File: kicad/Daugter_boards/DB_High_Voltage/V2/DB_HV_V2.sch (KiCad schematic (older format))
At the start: 5 parts, among them P1 CONN_01X19, P2 BNC, P3 CONN_01X19, U1 Recom

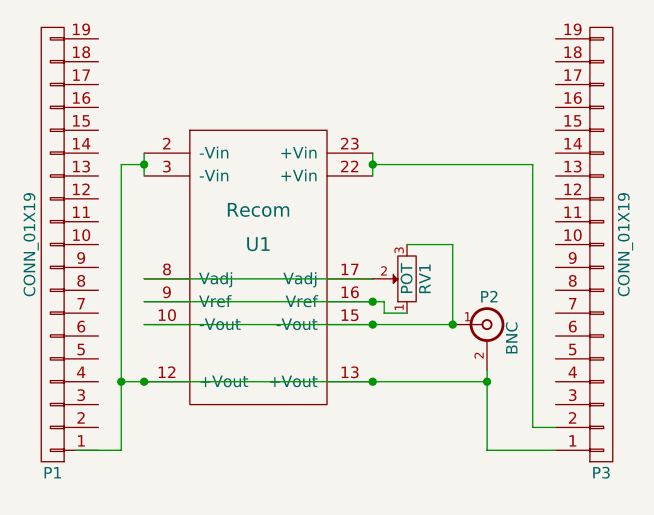
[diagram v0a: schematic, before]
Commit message: adding DB_Filter
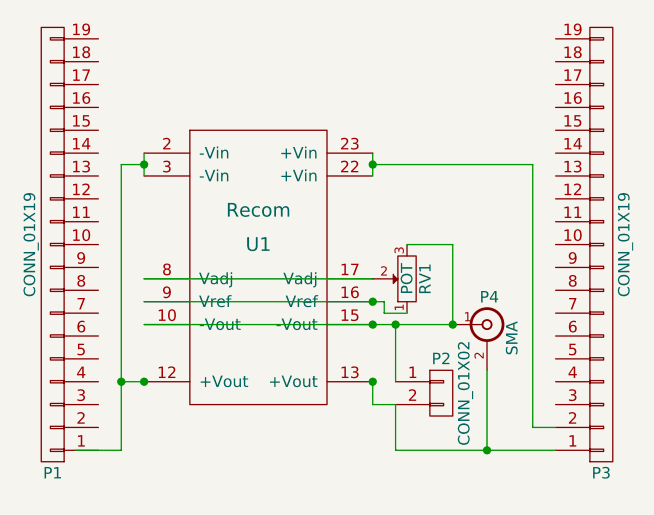
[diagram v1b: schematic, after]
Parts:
- removed P2: BNC, symbol BNC
- added P2: CONN_01X02, symbol CONN_01X02
- added P4: SMA, symbol SMA
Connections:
- wire segments 18 -> 22
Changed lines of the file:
@@
 LIBS:valves
 LIBS:echopen
+LIBS:DB_HV_V2-cache
 EELAYER 25 0
 EELAYER END
@@
 Wire Wire Line
 	4450 3350 5800 3350
-Wire Wire Line
-	4350 3600 5950 3600
 Wire Wire Line
 	4450 2650 4350 2650
@@
 	4350 3900 4150 3900
 Connection ~ 4350 3600
-$Comp
-L BNC P2
-U 1 1 57A84EE9
-P 5950 3350
-F 0 "P2" H 5960 3470 50  0000 C CNN
-F 1 "BNC" V 6060 3290 50  0000 C CNN
-F 2 "" H 5950 3350 50  0000 C CNN
-F 3 "" H 5950 3350 50  0000 C CNN
-	1    5950 3350
-	1    0    0    -1
-$EndComp
-Wire Wire Line
-	5950 3550 5950 3900
 Connection ~ 5450 3600
 $Comp
@@
 $EndComp
 Wire Wire Line
-	5950 3900 6250 3900
-Connection ~ 5950 3600
+	5550 3900 6250 3900
 Wire Wire Line
 	6150 2650 6150 3800
 Wire Wire Line
 	6150 3800 6250 3800
+$Comp
+L SMA P4
+U 1 1 57A87B90
+P 5950 3350
+F 0 "P4" H 5960 3470 50  0000 C CNN
+F 1 "SMA" V 6060 3290 50  0000 C CNN
+F 2 "" H 5950 3350 50  0000 C CNN
+F 3 "" H 5950 3350 50  0000 C CNN
+	1    5950 3350
+	1    0    0    -1
+$EndComp
+$Comp
+L CONN_01X02 P2
+U 1 1 57A87C25
+P 5750 3650
+F 0 "P2" H 5750 3800 50  0000 C CNN
+F 1 "CONN_01X02" V 5850 3650 50  0000 C CNN
+F 2 "" H 5750 3650 50  0000 C CNN
+F 3 "" H 5750 3650 50  0000 C CNN
+	1    5750 3650
+	1    0    0    -1
+$EndComp
+Wire Wire Line
+	5450 3600 5450 3700
+Wire Wire Line
+	5450 3700 5550 3700
+Wire Wire Line
+	5550 3700 5550 3900
+Wire Wire Line
+	5550 3350 5550 3600
+Connection ~ 5550 3350
+Wire Wire Line
+	5950 3550 5950 3900
+Connection ~ 5950 3900
+Wire Wire Line
+	4350 3600 4450 3600
 $EndSCHEMATC

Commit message: adding DB_HV
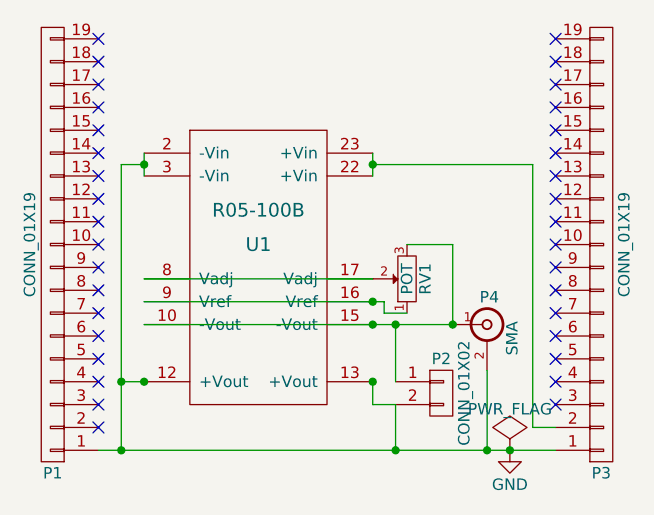
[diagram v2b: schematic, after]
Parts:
- P1, P3: footprint (none) -> Socket_Strips:Socket_Strip_Straight_1x19
- P2: footprint (none) -> Socket_Strips:Socket_Strip_Angled_1x02
- P4: footprint (none) -> Sockets_BNC:BNC_Socket_TYCO-AMP_LargePads
- RV1: footprint (none) -> Potentiometers:Potentiometer_Bourns_3296Y_3-8Zoll_Angular_ScrewUp
- U1: value Recom -> R05-100B; footprint (none) -> Converters_DCDC_ACDC:DCDC-Conv_TRACO_TED-1212_Single_9-18VDCto12VDC160mA
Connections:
- net labels added: GND
- wire segments 22 -> 21
- no-connect marks 0 -> 35
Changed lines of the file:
@@
 P 4950 3000
 F 0 "U1" H 4950 3000 60  0000 C CNN
-F 1 "Recom" H 4950 3150 60  0000 C CNN
-F 2 "" H 4650 3100 60  0000 C CNN
+F 1 "R05-100B" H 4950 3150 60  0000 C CNN
+F 2 "Converters_DCDC_ACDC:DCDC-Conv_TRACO_TED-1212_Single_9-18VDCto12VDC160mA" H 4650 3100 60  0001 C CNN
 F 3 "" H 4650 3100 60  0000 C CNN
 	1    4950 3000
@@
 F 0 "RV1" H 5600 3070 50  0000 C CNN
 F 1 "POT" H 5600 3150 50  0000 C CNN
-F 2 "" H 5600 3150 50  0000 C CNN
+F 2 "Potentiometers:Potentiometer_Bourns_3296Y_3-8Zoll_Angular_ScrewUp" H 5600 3150 50  0001 C CNN
 F 3 "" H 5600 3150 50  0000 C CNN
 	1    5600 3150
@@
 F 0 "P1" H 4050 4000 50  0000 C CNN
 F 1 "CONN_01X19" V 4150 3000 50  0000 C CNN
-F 2 "" H 4050 3000 50  0000 C CNN
+F 2 "Socket_Strips:Socket_Strip_Straight_1x19" H 4050 3000 50  0001 C CNN
 F 3 "" H 4050 3000 50  0000 C CNN
 	1    4050 3000
 	-1   0    0    1
 $EndComp
-Wire Wire Line
-	4350 3900 4150 3900
 Connection ~ 4350 3600
 Connection ~ 5450 3600
@@
 F 0 "P3" H 6450 4000 50  0000 C CNN
 F 1 "CONN_01X19" V 6550 3000 50  0000 C CNN
-F 2 "" H 6450 3000 50  0000 C CNN
+F 2 "Socket_Strips:Socket_Strip_Straight_1x19" H 6450 3000 50  0001 C CNN
 F 3 "" H 6450 3000 50  0000 C CNN
 	1    6450 3000
@@
 $EndComp
 Wire Wire Line
-	5550 3900 6250 3900
+	4250 3900 6250 3900
 Wire Wire Line
 	6150 2650 6150 3800
@@
 F 0 "P4" H 5960 3470 50  0000 C CNN
 F 1 "SMA" V 6060 3290 50  0000 C CNN
-F 2 "" H 5950 3350 50  0000 C CNN
+F 2 "Sockets_BNC:BNC_Socket_TYCO-AMP_LargePads" H 5950 3350 50  0001 C CNN
 F 3 "" H 5950 3350 50  0000 C CNN
 	1    5950 3350
@@
 F 0 "P2" H 5750 3800 50  0000 C CNN
 F 1 "CONN_01X02" V 5850 3650 50  0000 C CNN
-F 2 "" H 5750 3650 50  0000 C CNN
+F 2 "Socket_Strips:Socket_Strip_Angled_1x02" H 5750 3650 50  0001 C CNN
 F 3 "" H 5750 3650 50  0000 C CNN
 	1    5750 3650
@@
 Wire Wire Line
 	4350 3600 4450 3600
+$Comp
+L PWR_FLAG #FLG01
+U 1 1 57B2E414
+P 6050 3900
+F 0 "#FLG01" H 6050 3995 50  0001 C CNN
+F 1 "PWR_FLAG" H 6050 4080 50  0000 C CNN
+F 2 "" H 6050 3900 50  0000 C CNN
+F 3 "" H 6050 3900 50  0000 C CNN
+	1    6050 3900
+	1    0    0    -1
+$EndComp
+$Comp
+L GND #PWR02
+U 1 1 57B2E43A
+P 6050 3900
+F 0 "#PWR02" H 6050 3650 50  0001 C CNN
+F 1 "GND" H 6050 3750 50  0000 C CNN
+F 2 "" H 6050 3900 50  0000 C CNN
+F 3 "" H 6050 3900 50  0000 C CNN
+	1    6050 3900
+	1    0    0    -1
+$EndComp
+Connection ~ 6050 3900
+NoConn ~ 4250 2100
+NoConn ~ 4250 2200
+NoConn ~ 4250 2300
+NoConn ~ 4250 2400
+NoConn ~ 4250 2500
+NoConn ~ 4250 2600
+NoConn ~ 4250 2700
+NoConn ~ 4250 2800
+NoConn ~ 4250 2900
+NoConn ~ 4250 3000
+NoConn ~ 4250 3100
+NoConn ~ 4250 3200
+NoConn ~ 4250 3300
+NoConn ~ 4250 3400
+NoConn ~ 4250 3500
+NoConn ~ 4250 3600
+NoConn ~ 4250 3700
+NoConn ~ 4250 3800
+NoConn ~ 6250 3700
+NoConn ~ 6250 3600
+NoConn ~ 6250 3500
+NoConn ~ 6250 3400
+NoConn ~ 6250 3300
+NoConn ~ 6250 3200
+NoConn ~ 6250 3100
+NoConn ~ 6250 3000
+NoConn ~ 6250 2900
+NoConn ~ 6250 2800
+NoConn ~ 6250 2700
+NoConn ~ 6250 2600
+NoConn ~ 6250 2500
+NoConn ~ 6250 2400
+NoConn ~ 6250 2300
+NoConn ~ 6250 2200
+NoConn ~ 6250 2100
+Connection ~ 5550 3900
+Connection ~ 4350 3900
 $EndSCHEMATC
